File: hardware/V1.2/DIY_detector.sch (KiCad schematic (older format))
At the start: 36 parts, among them J1 Conn_01x02_Female, J2 Conn_01x02_Female, J3 BNC socket, SW1 -, U1 TLE2072

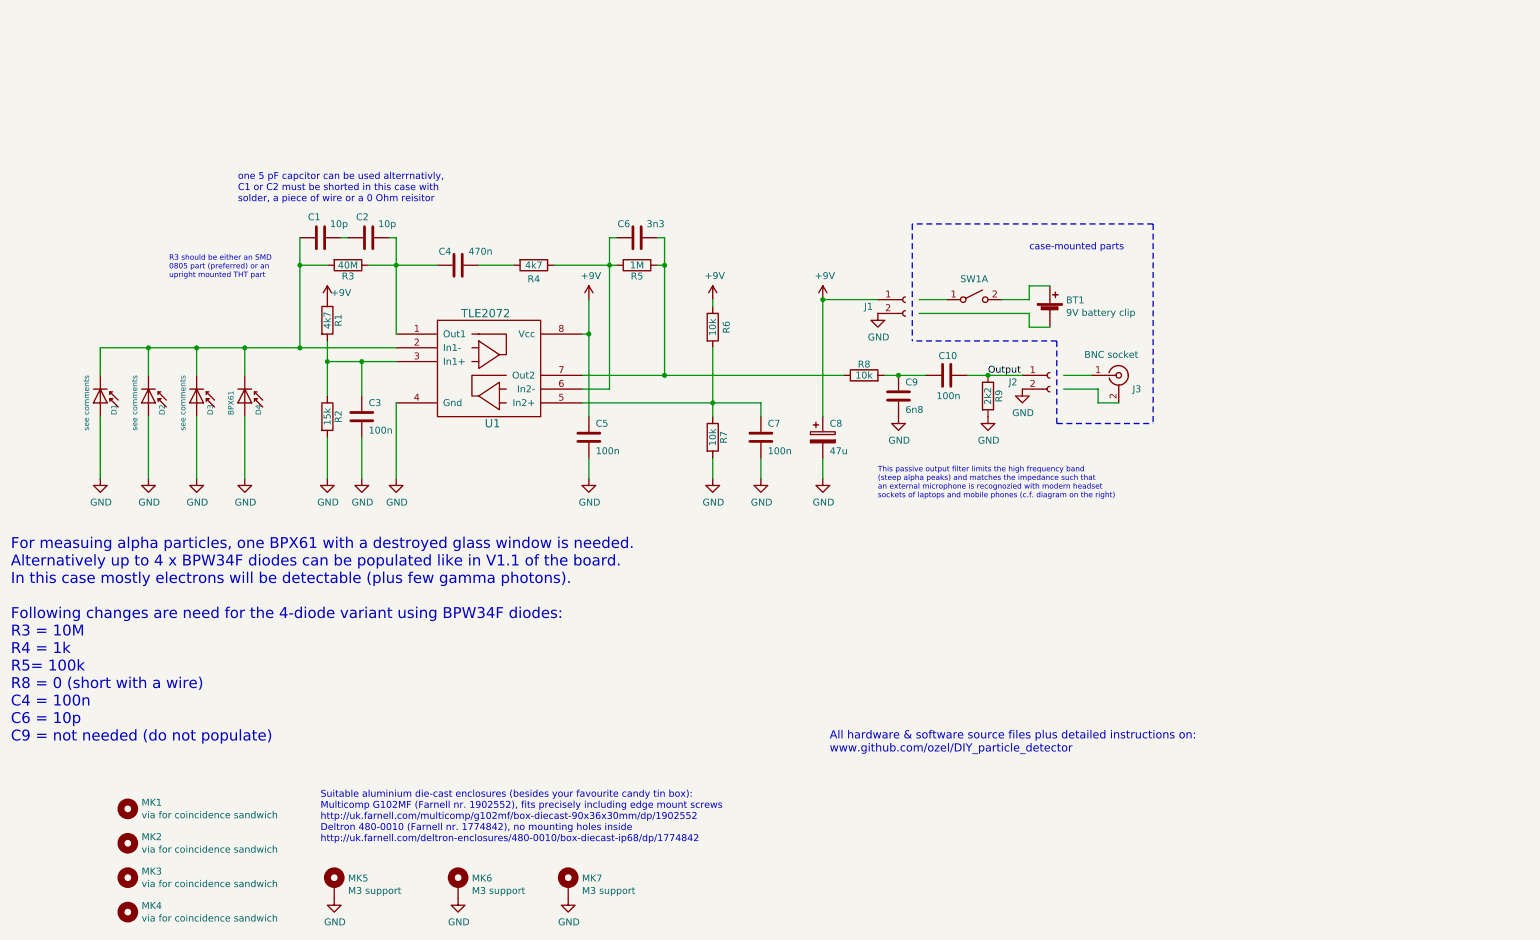
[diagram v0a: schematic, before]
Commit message: updating documentation and new parts overview sheets for assembly
updating PDF of schematic, gerber files of board layout, and fixing some typos as well
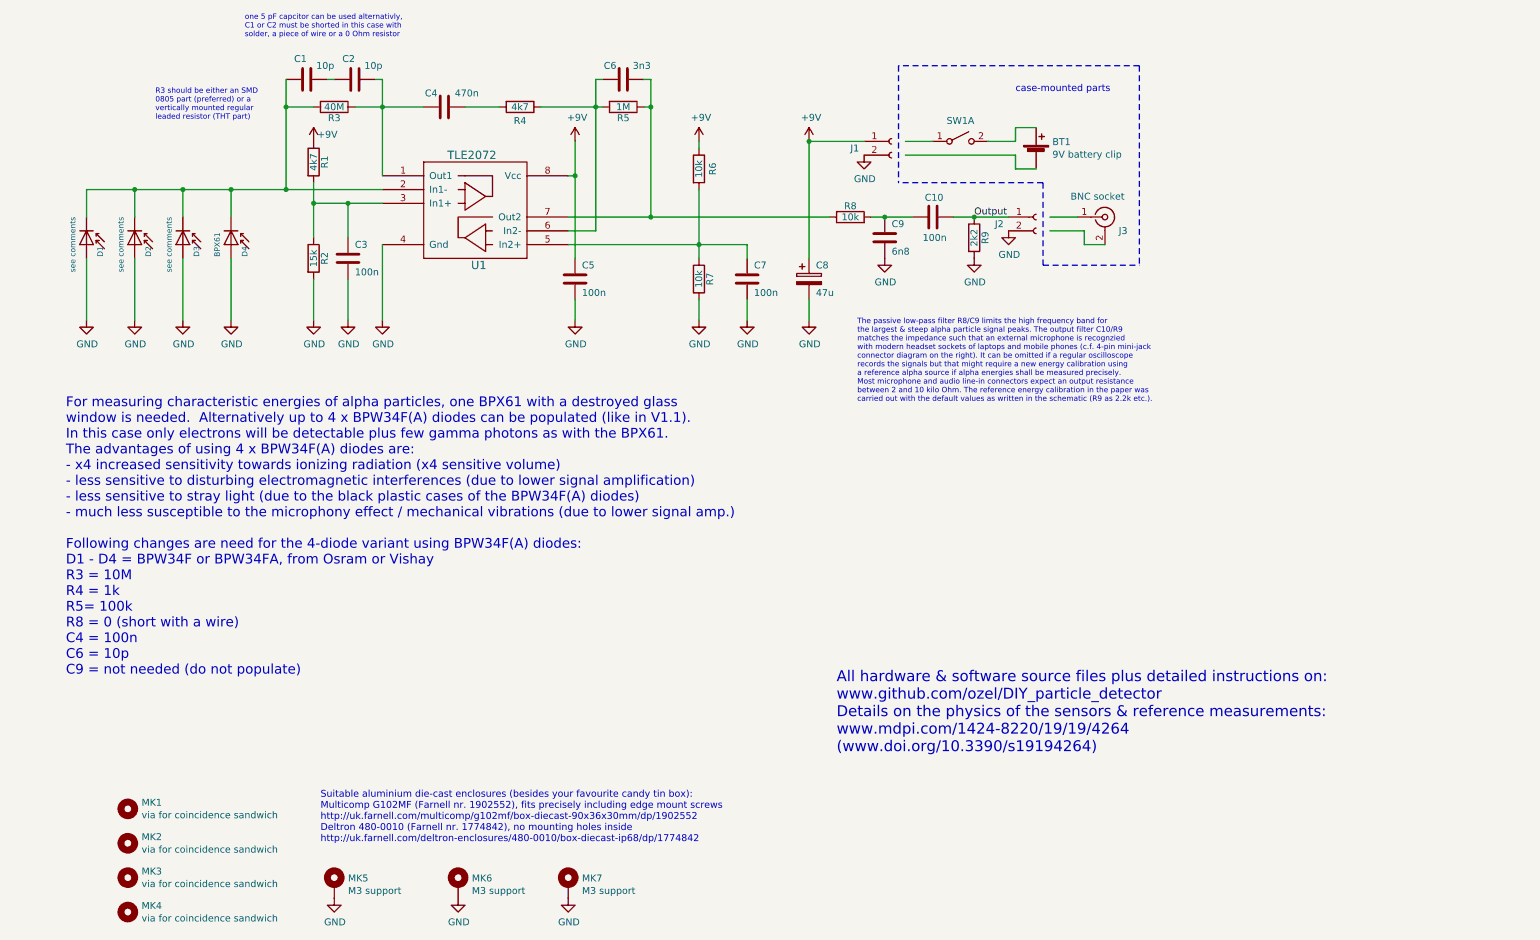
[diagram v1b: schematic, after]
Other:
- note added: "All hardware & software source files plus detailed instructions on:\nwww.github.com/ozel/DIY_particle_detector\nDetails on the physics of the sensors & reference measurements:\nwww.mdpi.com/1424-8220/19/19/4264 \n(www.doi.org/10.3390/s19194264)"
- note added: "For measuring characteristic energies of alpha particles, one BPX61 with a destroyed glass \nwindow is needed. Alternatively up to 4 x BPW34F(A) diodes can be populated (like in V1.1). \nIn this case only electrons will be detectable plus few gamma photons as with the BPX61. \nThe advantages of using 4 x BPW34F(A) diodes are: \n- x4 increased sensitivity towards ionizing radiation (x4 sensitive v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"
- note added: "R3 should be either an SMD \n0805 part (preferred) or a \nvertically mounted regular\nleaded resistor (THT part)\n"
- note added: "The passive low-pass filter R8/C9 limits the high frequency band for \nthe largest & steep alpha particle signal peaks. The output filter C10/R9 \nmatches the impedance such that an external microphone is recognzied\nwith modern headset sockets of laptops and mobile phones (c.f. 4-pin mini-jack \nconnector diagram on the right). It can be omitted if a regular oscilloscope \nrecords the signals bu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"
- note added: "one 5 pF capcitor can be used alternativly,\nC1 or C2 must be shorted in this case with \nsolder, a piece of wire or a 0 Ohm resistor"
- note removed: "All hardware & software source files plus detailed instructions on:\nwww.github.com/ozel/DIY_particle_detector"
- note removed: "For measuing alpha particles, one BPX61 with a destroyed glass window is needed. \nAlternatively up to 4 x BPW34F diodes can be populated like in V1.1 of the board. \nIn this case mostly electrons will be detectable (plus few gamma photons).\n\nFollowing changes are need for the 4-diode variant using BPW34F diodes:\nR3 = 10M\nR4 = 1k\nR5= 100k\nR8 = 0 (short with a wire)\nC4 = 100n\nC6 = 10p\nC9 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"
- note removed: "R3 should be either an SMD \n0805 part (preferred) or an \nupright mounted THT part\n"
- note removed: "This passive output filter limits the high frequency band\n(steep alpha peaks) and matches the impedance such that\nan external microphone is recognozied with modern headset \nsockets of laptops and mobile phones (c.f. diagram on the right)"
- note removed: "one 5 pF capcitor can be used alterrnativly,\nC1 or C2 must be shorted in this case with \nsolder, a piece of wire or a 0 Ohm reisitor"
- moved on the sheet: BT1, C1, C10, C2, C3, C4, C5, C6, C7, C8, C9, D1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

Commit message: BOM files in preparation for Kitspace release
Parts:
- BT1: FARNELL (none) -> 2817539; VENDOR Farnell -> (none); VENDOR_PN 2817539 -> (none)
- C1, C2: Description (none) -> 10pF THT; FARNELL (none) -> 1694175; VENDOR Farnell -> (none); VENDOR_PN 1694175 -> (none)
- C10, C3, C5, C7: Description (none) -> 100nF THT; FARNELL (none) -> 2112751; VENDOR Farnell -> (none); VENDOR_PN 2112751 -> (none)
- C4: Description (none) -> 470nf THT; FARNELL (none) -> 1457660; VENDOR Farnell -> (none); VENDOR_PN 1457660 -> (none)
- C6: Description (none) -> 3.3nF THT; FARNELL (none) -> 2901293; VENDOR Farnell -> (none); VENDOR_PN 2901293 -> (none)
- C8: Description (none) -> 47uF 63V THT; FARNELL (none) -> 9693033; VENDOR Farnell -> (none); VENDOR_PN 9693033 -> (none)
- C9: Description (none) -> 6.8nF THT; FARNELL (none) -> 2901297; VENDOR Farnell -> (none); VENDOR_PN 2901297 -> (none)
- D1, D2, D3: Description (none) -> silicon PIN photodiode; FARNELL (none) -> 2981621; RS Online (none) -> 654-7921; VENDOR Farnell -> (none); VENDOR2 RS Online -> (none); VENDOR2_PN 654-7921 -> (none); VENDOR_PN 2981621 -> (none)
- D4: Description (none) -> silicon PIN photodiode; FARNELL (none) -> 2981630; RS Online (none) -> 654-7785; VENDOR Farnell -> (none); VENDOR2 RS Online -> (none); VENDOR2_PN 654-7785 -> (none); VENDOR_PN 2981630 -> (none)
- J3: Description (none) -> male BNC wall socket; FARNELL (none) -> 1169699; VENDOR Farnell -> (none); VENDOR_PN 1169699 -> (none)
- R1: Description (none) -> 4.7k 1% THT; FARNELL (none) -> 2401772; VENDOR Farnell -> (none); VENDOR_PN 2401772 -> (none)
- R2: Description (none) -> 15k 1% THT; FARNELL (none) -> 2401785; VENDOR Farnell -> (none); VENDOR_PN 2401785 -> (none)
- R3: Description (none) -> 40Mega 10% 0805 SMD; FARNELL (none) -> 1174521; MFG Multicomp -> TE Connectivity; MFG_PN MCMF006FF1005A50 -> RH73H2A40MKTN; VENDOR Farnell -> (none); VENDOR_PN 2401834 -> (none)
- R4: Description (none) -> 4.7k 1% THT; FARNELL (none) -> 2401772; MFG_PN MCMF006FF1001A50 -> MCMF006FF4701A50; VENDOR Farnell -> (none); VENDOR_PN 2401753 -> (none)
- R5: Description (none) -> 1Mega 1% THT; FARNELL (none) -> 2401807; VENDOR Farnell -> (none); VENDOR_PN 2401807 -> (none)
- R6, R7, R8: Description (none) -> 10k 1% THT; FARNELL (none) -> 2401780; VENDOR Farnell -> (none); VENDOR_PN 2401780 -> (none)
- R9: Description (none) -> 2.2k 1% THT; FARNELL (none) -> 2401780; VENDOR Farnell -> (none); VENDOR_PN 2401780 -> (none)
- SW1: Description (none) -> SPDT switch on-none-on; FARNELL (none) -> 9473416; VENDOR Farnell -> (none); VENDOR_PN 9473416 -> (none)
- U1: Description (none) -> TLE2072CP/ACP; FARNELL (none) -> 3117956; MFG_PN TLE2072CP/ACP -> TLE2072ACP; VENDOR Farnell -> (none); VENDOR_PN 3117956 -> (none)

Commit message: renderings and 3D part models for both variants
including generated 3D models for all THT resistors, opamp chip model
with label. also created more accurate BPX61 TO-39 model.
Schematic and exported .xml BOM file have two new columns which store
part values and 3D model locations of the electron detector assembly
variant (VALUE_B, 3D_B)
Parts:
- C4: 3D_B (none) -> ${KIPRJMOD}/3D/C_Disc_D3.0mm_W1.6mm_P2.50mm.wrl; VALUE_B (none) -> 100n
- C6: 3D_B (none) -> ${KIPRJMOD}/3D/C_Disc_D3.0mm_W1.6mm_P2.50mm.wrl; VALUE_B (none) -> 10p
- C9: VALUE_B (none) -> DNP
- D1: value see comments -> BPX61; 3D_B (none) -> ${KIPRJMOD}/3D/BPW34F.wrl; VALUE_B (none) -> BPW34F
- D2, D3: value see comments -> DNP; 3D_B (none) -> ${KIPRJMOD}/3D/BPW34F.wrl; VALUE_B (none) -> BPW34F
- D4: value BPX61 -> DNP; 3D_B (none) -> ${KIPRJMOD}/3D/BPW34F.wrl; VALUE_B (none) -> BPW34F
- R3: 3D_B (none) -> ${KIPRJMOD}/3D/Resistors_THT_custom.3dshapes/res_5band_10M_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; VALUE_B (none) -> 10M
- R4: 3D_B (none) -> ${KIPRJMOD}/3D/Resistors_THT_custom.3dshapes/res_5band_1K_P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; VALUE_B (none) -> 1k
- R5: 3D_B (none) -> ${KIPRJMOD}/3D/Resistors_THT_custom.3dshapes/res_5band_100K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; VALUE_B (none) -> 100k
- R8: 3D_B (none) -> ${KIPRJMOD}/3D/jumper_wire_P10.16mm.wrl; VALUE_B (none) -> 0
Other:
- moved on the sheet: D1, D2, D3, D4
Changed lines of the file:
@@
 F 6 "1457660" H -1200 -1550 50  0001 C CNN "FARNELL"
 F 7 "470nf THT" H 4200 1650 50  0001 C CNN "Description"
+F 8 "100n" H 4200 1650 50  0001 C CNN "VALUE_B"
+F 9 "${KIPRJMOD}/3D/C_Disc_D3.0mm_W1.6mm_P2.50mm.wrl" H 4200 1650 50  0001 C CNN "3D_B"
 	1    4200 1650
 	0    -1   -1   0
@@
 F 6 "2401807" H -1300 -1550 50  0001 C CNN "FARNELL"
 F 7 "1Mega 1% THT" H 5500 1650 50  0001 C CNN "Description"
+F 8 "100k" H 5500 1650 50  0001 C CNN "VALUE_B"
+F 9 "${KIPRJMOD}/3D/Resistors_THT_custom.3dshapes/res_5band_100K_P7.62mm.wrl" H 5500 1650 50  0001 C CNN "3D_B"
 	1    5500 1650
 	0    1    1    0
@@
 F 6 "2401772" H -1200 -1550 50  0001 C CNN "FARNELL"
 F 7 "4.7k 1% THT" H 4750 1650 50  0001 C CNN "Description"
+F 8 "1k" H 4750 1650 50  0001 C CNN "VALUE_B"
+F 9 "${KIPRJMOD}/3D/Resistors_THT_custom.3dshapes/res_5band_1K_P7.62mm.wrl" H 4750 1650 50  0001 C CNN "3D_B"
 	1    4750 1650
 	0    1    1    0
@@
 F 6 "1174521" H 3400 1650 50  0001 C CNN "FARNELL"
 F 7 "40Mega 10% 0805 SMD" H 3400 1650 50  0001 C CNN "Description"
+F 8 "10M" H 3400 1650 50  0001 C CNN "VALUE_B"
+F 9 "${KIPRJMOD}/3D/Resistors_THT_custom.3dshapes/res_5band_10M_P2.54mm.wrl" H 3400 1650 50  0001 C CNN "3D_B"
 	1    3400 1650
 	0    1    1    0
@@
 L Sensor_Optical:BPW34 D4
 U 1 1 4FA6949D
-P 2650 2650
-F 0 "D4" H 2700 2750 40  0000 C CNN
-F 1 "BPX61" H 2650 2550 40  0000 C CNN
-F 2 "Opto-Devices:PhotoDiode_DIL2_4.3x4.65_RM5.08" H 2650 2650 50  0001 C CNN
-F 3 "" H 2650 2650 50  0001 C CNN
-F 4 "Osram" H 2650 2650 50  0001 C CNN "MFG"
-F 5 "BPX61" H 2650 2650 50  0001 C CNN "MFG_PN"
-F 6 "2981630" H 2650 2650 50  0001 C CNN "FARNELL"
-F 7 "654-7785" H 2650 2650 50  0001 C CNN "RS Online"
-F 8 "silicon PIN photodiode" H 2650 2650 50  0001 C CNN "Description"
-	1    2650 2650
+P 1600 2650
+F 0 "D4" H 1650 2750 40  0000 C CNN
+F 1 "DNP" H 1600 2550 40  0000 C CNN
+F 2 "Opto-Devices:PhotoDiode_DIL2_4.3x4.65_RM5.08" H 1600 2650 50  0001 C CNN
+F 3 "" H 1600 2650 50  0001 C CNN
+F 4 "Osram" H 1600 2650 50  0001 C CNN "MFG"
+F 5 "BPX61" H 1600 2650 50  0001 C CNN "MFG_PN"
+F 6 "2981630" H 1600 2650 50  0001 C CNN "FARNELL"
+F 7 "654-7785" H 1600 2650 50  0001 C CNN "RS Online"
+F 8 "silicon PIN photodiode" H 1600 2650 50  0001 C CNN "Description"
+F 9 "${KIPRJMOD}/3D/BPW34F.wrl" H 1600 2650 50  0001 C CNN "3D_B"
+F 10 "BPW34F" H 1600 2650 50  0001 C CNN "VALUE_B"
+	1    1600 2650
 	0    1    1    0
 $EndComp
@@
 F 6 "2901293" H 5500 1450 50  0001 C CNN "FARNELL"
 F 7 "3.3nF THT" H 5500 1450 50  0001 C CNN "Description"
+F 8 "10p" H 5500 1450 50  0001 C CNN "VALUE_B"
+F 9 "${KIPRJMOD}/3D/C_Disc_D3.0mm_W1.6mm_P2.50mm.wrl" H 5500 1450 50  0001 C CNN "3D_B"
 	1    5500 1450
 	0    -1   -1   0
@@
 L Sensor_Optical:BPW34 D3
 U 1 1 5AFA9712
+P 1950 2650
+F 0 "D3" H 2000 2750 40  0000 C CNN
+F 1 "DNP" H 1950 2550 40  0000 C CNN
+F 2 "Opto-Devices:PhotoDiode_DIL2_4.3x4.65_RM5.08" H 1950 2650 50  0001 C CNN
+F 3 "" H 1950 2650 50  0001 C CNN
+F 4 "Osram/Vishay" H 1950 2650 50  0001 C CNN "MFG"
+F 5 "BPW34F/FA" H 1950 2650 50  0001 C CNN "MFG_PN"
+F 6 "2981621" H 1950 2650 50  0001 C CNN "FARNELL"
+F 7 "654-7921" H 1950 2650 50  0001 C CNN "RS Online"
+F 8 "silicon PIN photodiode" H 1950 2650 50  0001 C CNN "Description"
+F 9 "${KIPRJMOD}/3D/BPW34F.wrl" H 1950 2650 50  0001 C CNN "3D_B"
+F 10 "BPW34F" H 1950 2650 50  0001 C CNN "VALUE_B"
+	1    1950 2650
+	0    1    1    0
+$EndComp
+$Comp
+L Sensor_Optical:BPW34 D2
+U 1 1 5AFA9764
 P 2300 2650
-F 0 "D3" H 2350 2750 40  0000 C CNN
-F 1 "see comments" H 2300 2550 40  0000 C CNN
+F 0 "D2" H 2350 2750 40  0000 C CNN
+F 1 "DNP" H 2300 2550 40  0000 C CNN
 F 2 "Opto-Devices:PhotoDiode_DIL2_4.3x4.65_RM5.08" H 2300 2650 50  0001 C CNN
 F 3 "" H 2300 2650 50  0001 C CNN
@@
 F 7 "654-7921" H 2300 2650 50  0001 C CNN "RS Online"
 F 8 "silicon PIN photodiode" H 2300 2650 50  0001 C CNN "Description"
+F 9 "${KIPRJMOD}/3D/BPW34F.wrl" H 2300 2650 50  0001 C CNN "3D_B"
+F 10 "BPW34F" H 2300 2650 50  0001 C CNN "VALUE_B"
 	1    2300 2650
 	0    1    1    0
 $EndComp
 $Comp
-L Sensor_Optical:BPW34 D2
-U 1 1 5AFA9764
-P 1950 2650
-F 0 "D2" H 2000 2750 40  0000 C CNN
-F 1 "see comments" H 1950 2550 40  0000 C CNN
-F 2 "Opto-Devices:PhotoDiode_DIL2_4.3x4.65_RM5.08" H 1950 2650 50  0001 C CNN
-F 3 "" H 1950 2650 50  0001 C CNN
-F 4 "Osram/Vishay" H 1950 2650 50  0001 C CNN "MFG"
-F 5 "BPW34F/FA" H 1950 2650 50  0001 C CNN "MFG_PN"
-F 6 "2981621" H 1950 2650 50  0001 C CNN "FARNELL"
-F 7 "654-7921" H 1950 2650 50  0001 C CNN "RS Online"
-F 8 "silicon PIN photodiode" H 1950 2650 50  0001 C CNN "Description"
-	1    1950 2650
-	0    1    1    0
-$EndComp
-$Comp
 L Sensor_Optical:BPW34 D1
 U 1 1 5AFA97B6
-P 1600 2650
-F 0 "D1" H 1650 2750 40  0000 C CNN
-F 1 "see comments" H 1600 2550 40  0000 C CNN
-F 2 "Opto-Devices:PhotoDiode_DIL2_4.3x4.65_RM5.08" H 1600 2650 50  0001 C CNN
-F 3 "" H 1600 2650 50  0001 C CNN
-F 4 "Osram/Vishay" H 1600 2650 50  0001 C CNN "MFG"
-F 5 "BPW34F/FA" H 1600 2650 50  0001 C CNN "MFG_PN"
-F 6 "2981621" H 1600 2650 50  0001 C CNN "FARNELL"
-F 7 "654-7921" H 1600 2650 50  0001 C CNN "RS Online"
-F 8 "silicon PIN photodiode" H 1600 2650 50  0001 C CNN "Description"
-	1    1600 2650
+P 2650 2650
+F 0 "D1" H 2700 2750 40  0000 C CNN
+F 1 "BPX61" H 2650 2550 40  0000 C CNN
+F 2 "Opto-Devices:PhotoDiode_DIL2_4.3x4.65_RM5.08" H 2650 2650 50  0001 C CNN
+F 3 "" H 2650 2650 50  0001 C CNN
+F 4 "Osram/Vishay" H 2650 2650 50  0001 C CNN "MFG"
+F 5 "BPW34F/FA" H 2650 2650 50  0001 C CNN "MFG_PN"
+F 6 "2981621" H 2650 2650 50  0001 C CNN "FARNELL"
+F 7 "654-7921" H 2650 2650 50  0001 C CNN "RS Online"
+F 8 "silicon PIN photodiode" H 2650 2650 50  0001 C CNN "Description"
+F 9 "${KIPRJMOD}/3D/BPW34F.wrl" H 2650 2650 50  0001 C CNN "3D_B"
+F 10 "BPW34F" H 2650 2650 50  0001 C CNN "VALUE_B"
+	1    2650 2650
 	0    1    1    0
 $EndComp
@@
 $EndComp
 Text Notes 1450 5900 0    71   ~ 0
-For measuring characteristic energies of alpha particles, one BPX61 with a destroyed glass \nwindow is needed.  Alternatively up to 4 x BPW34F(A) diodes can be populated (like in V1.1). \nIn this case only electrons will be detectable plus few gamma photons as with the BPX61. \nThe advantages of using 4 x BPW34F(A) diodes are: \n- x4 increased sensitivity towards ionizing radiation (x4 sensitive volume)\n- less sensitive to disturbing electromagnetic interferences (due to lower signal amplification)\n- less sensitive to stray light (due to the black plastic cases of the BPW34F(A) diodes)\n- much less susceptible to the microphony effect / mechanical vibrations (due to lower signal amp.)\n\nFollowing changes are need for the 4-diode variant using BPW34F(A) diodes:\nD1 - D4 = BPW34F or BPW34FA, from Osram or Vishay\nR3 = 10M\nR4 = 1k\nR5 = 100k\nR8 = 0 (short with a wire)\nC4 = 100n\nC6 = 10p\nC9 = not needed (do not populate)\n\n
+For measuring characteristic energies of alpha particles, one BPX61 with a destroyed glass \nwindow is needed.  Alternatively up to 4 x BPW34F(A) diodes can be populated (like in V1.1). \nIn this case only electrons will be detectable plus few gamma photons as with the BPX61. \nThe advantages of using 4 x BPW34F(A) diodes are: \n- x4 increased sensitivity towards ionizing radiation (x4 sensitive volume)\n- less sensitive to disturbing electromagnetic interferences (due to lower signal amplification)\n- less sensitive to stray light (due to the black plastic cases of the BPW34F(A) diodes)\n- much less susceptible to the microphony effect / mechanical vibrations (due to lower signal amp.)\n\nFollowing changes are need for the 4-diode variant using BPW34F(A) diodes:\nD1 - D4 = BPW34F or BPW34FA, from Osram or Vishay\nR3 = 10M\nR4 = 1k\nR5 = 100k\nR8 = 0 (short with a wire)\nC4 = 100n\nC6 = 10p\nC9 = not needed (DNP = do not populate)\n\n
 $Comp
 L Device:R R8
@@
 F 6 "2401780" H -100 -1950 50  0001 C CNN "FARNELL"
 F 7 "10k 1% THT" H 7150 2450 50  0001 C CNN "Description"
+F 8 "0" H 7150 2450 50  0001 C CNN "VALUE_B"
+F 9 "${KIPRJMOD}/3D/jumper_wire_P10.16mm.wrl" H 7150 2450 50  0001 C CNN "3D_B"
 	1    7150 2450
 	0    -1   -1   0
@@
 F 6 "2901297" H -1500 -1800 50  0001 C CNN "FARNELL"
 F 7 "6.8nF THT" H 7400 2600 50  0001 C CNN "Description"
+F 8 "DNP" H 7400 2600 50  0001 C CNN "VALUE_B"
 	1    7400 2600
 	1    0    0    -1
